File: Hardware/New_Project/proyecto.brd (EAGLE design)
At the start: 25.1 x 39.5 mm, 45 parts, among them J1 USB4105-GF-A, Q1 DMP1045U, U1 ESP32C3_QFN32X5, U2 MPU-6050, U3 MCP73831-2ACI/MC, Y1 ABM11W-101-32.0000MHZ-T3

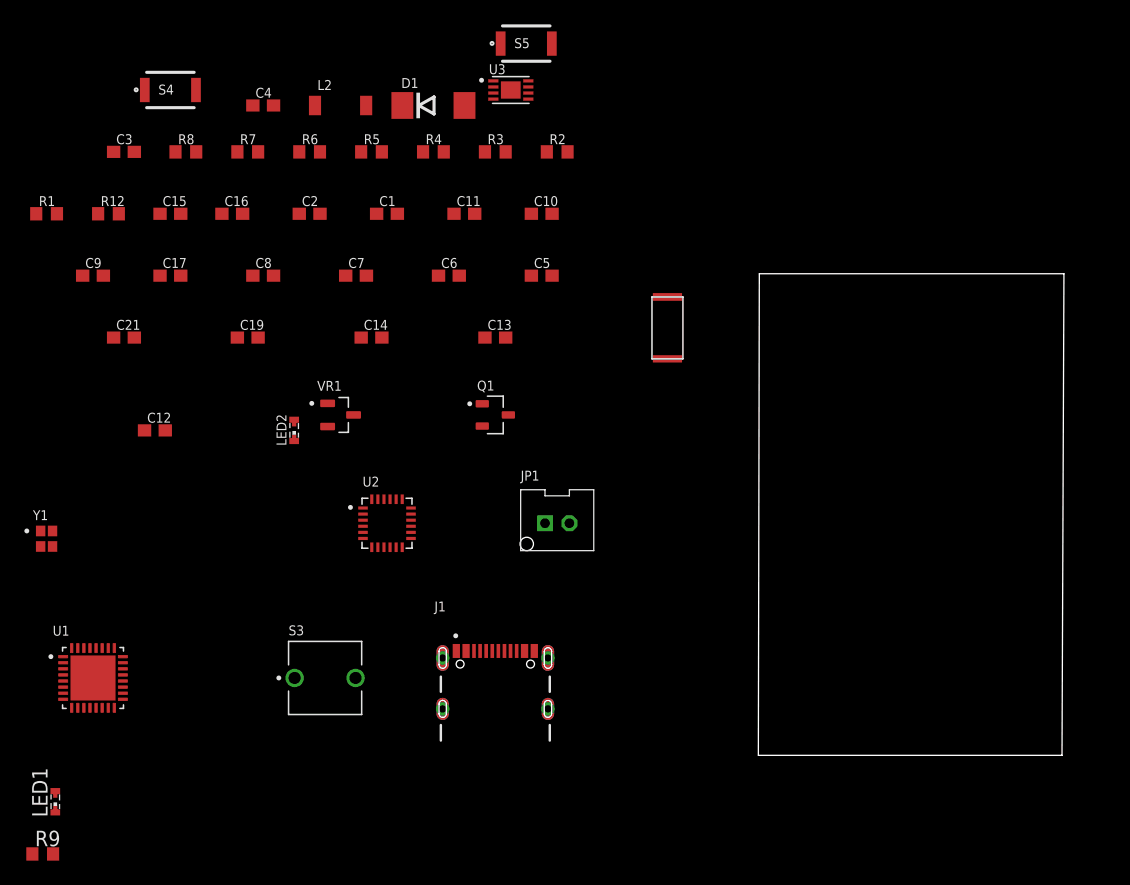
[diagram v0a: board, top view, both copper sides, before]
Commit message: Se agrega el diseño corregido
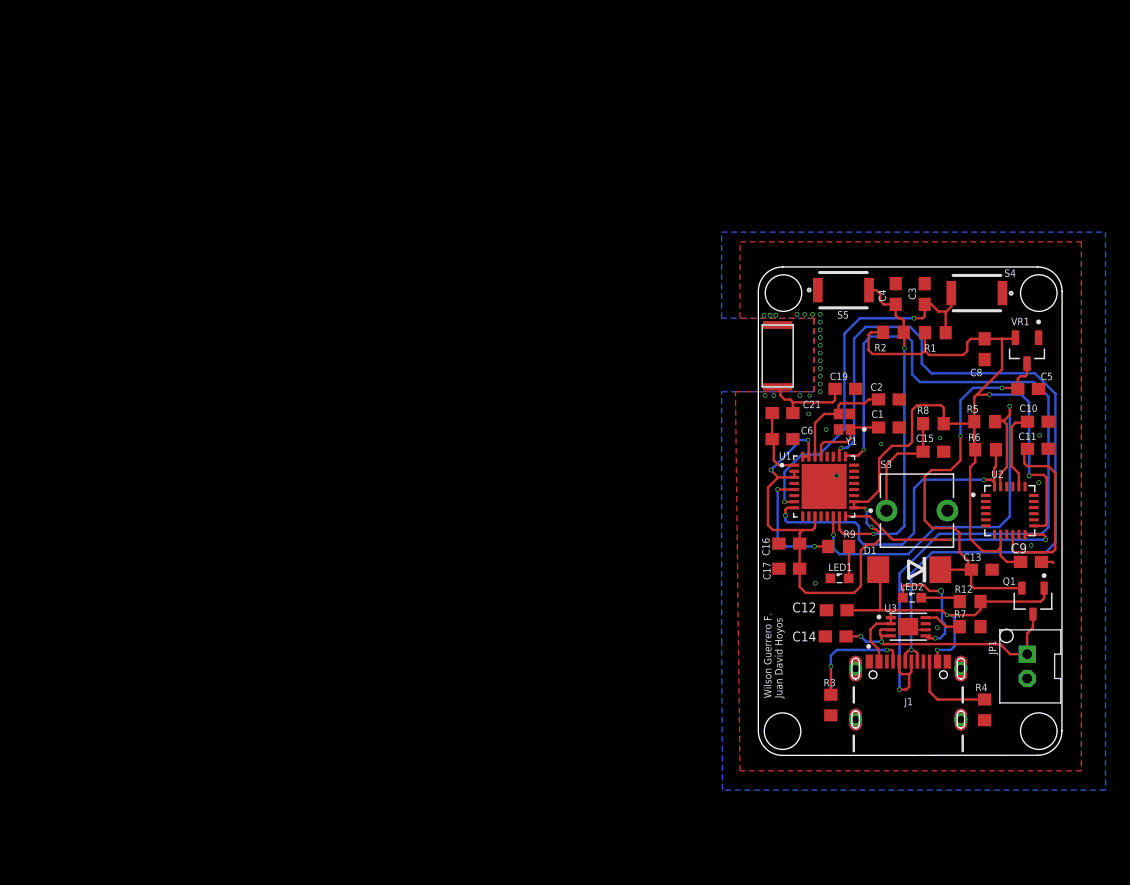
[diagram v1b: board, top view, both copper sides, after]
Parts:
- removed C7: 100nF, rcl:C0603
- removed L2: (no value), rcl:L4516C
- C5: value 100nF -> 10uF
- C6: value 100nF -> 4.7uF/10V
- C8: value 100nF -> 1uF
- LED1, LED2: device led:SMARTLED-TTW -> led:SML0603
- moved C9 80.5 mm to (22.4, 15.9)
- moved R12 77.6 mm to (17.4, 12.6)
- moved R1 73.6 mm to (14.5, 34.7), turned to 180 degrees
- moved R7 71.0 mm to (17.4, 10.6), turned to 180 degrees
- moved R9 70.0 mm to (6.59, 17.1), turned to 180 degrees
- moved S4 68.3 mm to (17.9, 37.9), turned to 180 degrees
- moved LED1 66.9 mm to (6.67, 14.5)
- moved C3 66.8 mm to (13.7, 37.9), turned to 90 degrees
- moved Y1 66.2 mm to (7.06, 27.4), turned to 180 degrees
- moved C15 65.6 mm to (14.4, 24.9)
- moved R8 65.3 mm to (14.4, 27.2)
- moved R4 64.4 mm to (18.6, 3.73), turned to 90 degrees
- moved U1 62.0 mm to (5.40, 22.1)
- moved R6 60.6 mm to (18.7, 25.1), turned to 180 degrees
- moved C8 59.5 mm to (18.6, 33.3), turned to 270 degrees
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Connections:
- net +3V3: no longer C7.1
- net 5V_F: no longer C6.1
- net ANT: now also C6.1; no longer L2.1
- net GND: now also LED1.C; no longer C7.2, L2.2, LED1.C@1
- net N$1: now also LED1.A; no longer LED1.A@1
- net N$3: now also LED2.A; no longer LED2.A@1
- net N$4: now also LED2.C; no longer LED2.C@1
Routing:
- net +3V3: track 0.00 -> 114.5 mm, vias 0 -> 6
- net USB_D-: track 0.00 -> 68.3 mm, vias 0 -> 2
- net USB_D+: track 0.00 -> 64.8 mm, vias 0 -> 2
- net SCL: track 0.00 -> 35.6 mm, vias 0 -> 2
- net 5V_F: track 0.00 -> 34.5 mm, vias 0 -> 2
- net +5V: track 0.00 -> 33.0 mm, vias 0 -> 2
- net RESET: track 0.00 -> 31.1 mm, vias 0 -> 2
- net BOOT: track 0.00 -> 28.5 mm, vias 0 -> 2
- net SDA: track 0.00 -> 27.8 mm, vias 0 -> 2
- net BAT: track 0.00 -> 21.6 mm, vias 0 -> 2
- net INT_ACELEROMETRO: track 0.00 -> 19.2 mm, vias 0 -> 2
- net N$8: track 0.00 -> 15.4 mm
- net +5V1: track 0.00 -> 9.78 mm, vias 0 -> 2
- net N$4: track 0.00 -> 9.74 mm, vias 0 -> 2
- net IOTBOT: track 0.00 -> 9.52 mm
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- added copper zone on layer 1, net GND
- added copper zone on layer 16, net GND
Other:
- board size 25.1 x 39.5 mm -> 24.9 x 40.1 mm
- board text added: "Wilson Guerrero F. Juan David Hoyos"
